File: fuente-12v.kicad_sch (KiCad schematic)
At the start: 36 parts, among them Q1 IPP65R190C7, Q2 CSD16403Q5A, U1 UCC287501D, U2 TCMT1107, U3 TL432DBZ, U4 TPS24701DGKR

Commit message: Esquematico completo y PCB routeado
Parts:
- removed C6: C, symbol Device:C_Polarized
- removed D1: D_Schottky, Package_TO_SOT_THT:TO-220-2_Vertical, symbol Device:D_Schottky
- added C13, C19: 10n, Capacitor_SMD:C_0805_2012Metric_Pad1.18x1.45mm_HandSolder, symbol Device:C
- added C14: 100uF, Capacitor_THT:CP_Radial_D8.0mm_P3.80mm, symbol Device:C
- added C15: 4.7uF 50V, Capacitor_SMD:C_0805_2012Metric_Pad1.18x1.45mm_HandSolder, symbol Device:C
- added C16: 470nF, Capacitor_SMD:C_0805_2012Metric_Pad1.18x1.45mm_HandSolder, symbol Device:C
- added C17: 470nF 400V, Capacitor_THT:C_Disc_D14.5mm_W5.0mm_P7.50mm, symbol Device:C
- added C20: 33nF X2, Capacitor_THT:C_Rect_L11.5mm_W6.6mm_P10.00mm_MKT, symbol Device:C
- added C21, C23: 100nF, Capacitor_SMD:C_0805_2012Metric_Pad1.18x1.45mm_HandSolder, symbol Device:C
- added C22: 470pF, Capacitor_SMD:C_0805_2012Metric_Pad1.18x1.45mm_HandSolder, symbol Device:C
- added C24: 10nF, Capacitor_SMD:C_1206_3216Metric_Pad1.33x1.80mm_HandSolder, symbol Device:C
- added C25, C26: 1nF Y1, Capacitor_THT:C_Disc_D10.5mm_W5.0mm_P10.00mm, symbol Device:C
- added C27: 22pF 50V, Capacitor_SMD:C_0805_2012Metric_Pad1.18x1.45mm_HandSolder, symbol Device:C
- added C29: 150uF 400V, Capacitor_THT:CP_Radial_D18.0mm_P7.50mm, symbol Device:C_Polarized
- added D1: GREEN, LED_SMD:LED_0805_2012Metric_Pad1.15x1.40mm_HandSolder, symbol Device:LED
- added D2, D3, D4, D5: 1N4148WT, Diode_SMD:D_SOD-523, symbol Diode:1N4148WT
- added D6: MBR20200CT, Package_TO_SOT_THT:TO-220-3_Vertical, symbol Device:D_Schottky_AKA
- added D7: Bzt52c20, Diode_SMD:Nexperia_CFP3_SOD-123W, symbol Device:D_Zener
- added D8: ES1J, Diode_SMD:D_SMA_Handsoldering, symbol Device:D
- added D9: KBL10, Diode_THT:Diode_Bridge_19.0x3.5x10.0mm_P5.0mm, symbol Device:D_Bridge_+AA-
- added F1: 1A 20mm, Fuse:Fuseholder_Cylinder-5x20mm_Schurter_0031_8201_Horizontal_Open, symbol Device:Fuse
- added FL1: ST-110BH, fuente-12v:ST-110, symbol Device:Filter_EMI_LL
- added J1: Conn_01x03_Pin, Connector_PinHeader_2.54mm:PinHeader_1x03_P2.54mm_Vertical, symbol Connector:Conn_01x03_Pin
- added J2: Screw_Terminal_01x03, TerminalBlock:TerminalBlock_MaiXu_MX126-5.0-03P_1x03_P5.00mm, symbol Connector:Screw_Terminal_01x03
- added J3: Conn_01x02_Pin, Connector_PinHeader_2.54mm:PinHeader_1x02_P2.54mm_Horizontal, symbol Connector:Conn_01x02_Pin
- added J5: OUTPUT, TerminalBlock:TerminalBlock_MaiXu_MX126-5.0-02P_1x02_P5.00mm, symbol Connector:Screw_Terminal_01x02
- added J6: Screw_Terminal_01x03 P5mm, TerminalBlock:TerminalBlock_MaiXu_MX126-5.0-03P_1x03_P5.00mm, symbol Connector:Screw_Terminal_01x03
- added R16: 0.018, Resistor_SMD:R_2512_6332Metric_Pad1.40x3.35mm_HandSolder, symbol Device:R
- added R17: 1M, Resistor_THT:R_Axial_DIN0207_L6.3mm_D2.5mm_P10.16mm_Horizontal, symbol Device:R
- added R18, R19: 2M, Resistor_SMD:R_0805_2012Metric_Pad1.20x1.40mm_HandSolder, symbol Device:R
- added R20, R21, R27: 10, Resistor_SMD:R_0805_2012Metric_Pad1.20x1.40mm_HandSolder, symbol Device:R
- added R22: 22, Resistor_SMD:R_1206_3216Metric_Pad1.30x1.75mm_HandSolder, symbol Device:R
- added R23: 80k, Resistor_SMD:R_1206_3216Metric_Pad1.30x1.75mm_HandSolder, symbol Device:R
- added R24: 6.8k, Resistor_SMD:R_0805_2012Metric_Pad1.20x1.40mm_HandSolder, symbol Device:R
- added R26: 10k, Resistor_SMD:R_0805_2012Metric_Pad1.20x1.40mm_HandSolder, symbol Device:R
- added RA1, RB1: 220, Resistor_SMD:R_0805_2012Metric_Pad1.20x1.40mm_HandSolder, symbol Device:R
- added RV1: 1k, Potentiometer_THT:Potentiometer_Bourns_3266Y_Vertical, symbol Device:R_Potentiometer_Trim
- added RV2: Varistor, Capacitor_THT:C_Disc_D8.0mm_W2.5mm_P5.00mm, symbol Device:Varistor
- added TP1, TP2, TP3, TP5, TP6, TP7, TP8, TP9: TestPoint, Connector_PinHeader_1.00mm:PinHeader_1x01_P1.00mm_Vertical, symbol Connector:TestPoint
- added U5: NE555P, Package_DIP:DIP-8_W7.62mm, symbol Timer:NE555P
- C1, C9: value C -> 680pF; footprint (none) -> Capacitor_SMD:C_0805_2012Metric_Pad1.18x1.45mm_HandSolder
- C10: value C -> 56pF; footprint (none) -> Capacitor_SMD:C_0805_2012Metric_Pad1.18x1.45mm_HandSolder
- C11: value C -> 1nF; footprint (none) -> Capacitor_SMD:C_0805_2012Metric_Pad1.18x1.45mm_HandSolder
- C12: value C -> 56nF; footprint (none) -> Capacitor_SMD:C_0805_2012Metric_Pad1.18x1.45mm_HandSolder
- C2, C3, C7: value C -> 4.7uF; footprint (none) -> Capacitor_SMD:C_1206_3216Metric_Pad1.33x1.80mm_HandSolder
- C4, C5: value C -> 470u; footprint (none) -> Capacitor_THT:CP_Radial_D13.0mm_P5.00mm
- C8: value 1nF -> 1nF Y1; footprint (none) -> Capacitor_THT:C_Disc_D16.0mm_W5.0mm_P10.00mm
- L1: value L -> 10uH 3A; footprint (none) -> Inductor_THT:L_Toroid_Vertical_L16.0mm_W8.0mm_P7.62mm
- R1: value R -> 10; footprint (none) -> Resistor_SMD:R_0805_2012Metric_Pad1.20x1.40mm_HandSolder
- R10: value R -> 5k; footprint (none) -> Resistor_SMD:R_0805_2012Metric_Pad1.20x1.40mm_HandSolder
- R11: value R -> 133k; footprint (none) -> Resistor_SMD:R_0805_2012Metric_Pad1.20x1.40mm_HandSolder
- R12: value R -> 2.49k; footprint (none) -> Resistor_SMD:R_0805_2012Metric_Pad1.20x1.40mm_HandSolder
- R13: value R -> 120k; footprint (none) -> Resistor_SMD:R_0805_2012Metric_Pad1.20x1.40mm_HandSolder
- R14, R5: value R -> 10k; footprint (none) -> Resistor_SMD:R_0805_2012Metric_Pad1.20x1.40mm_HandSolder
- R15: value R -> 0.018; footprint (none) -> Resistor_SMD:R_2512_6332Metric_Pad1.40x3.35mm_HandSolder
- R2, R4: value R -> 0.47; footprint (none) -> Resistor_SMD:R_2512_6332Metric_Pad1.40x3.35mm_HandSolder
- R3: value R -> 2M; footprint (none) -> Resistor_SMD:R_0805_2012Metric_Pad1.20x1.40mm_HandSolder
- R6: value R -> 100; footprint (none) -> Resistor_SMD:R_0805_2012Metric_Pad1.20x1.40mm_HandSolder
- R7: value R -> 51; footprint (none) -> Resistor_SMD:R_0805_2012Metric_Pad1.20x1.40mm_HandSolder
- R8: value R -> 86.6k; footprint (none) -> Resistor_SMD:R_0805_2012Metric_Pad1.20x1.40mm_HandSolder
- R9: value R -> 23.4k; footprint (none) -> Resistor_SMD:R_0805_2012Metric_Pad1.20x1.40mm_HandSolder
- T1: footprint (none) -> fuente-12v:750811744
- U4: footprint Package_TO_SOT_SMD:TSOT-23-6_HandSoldering -> Package_SO:VSSOP-8_2.3x2mm_P0.5mm
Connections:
- net FB: now also TP7.1
- net SECGND: now also R9.1, C16.1, J5.1 (Pin_1)
- net 12V: now reaches C5.1, L1.2, R14.2, R15.2, R7.2, U4.8 (VCC)
- net 12V: now also C3.2, R16.2, R24.1, TP3.1; no longer C7.2
- net at Q1.1 (G), R5.2: now also J1.2 (Pin_2); no longer R1.2
- net at Q1.2 (D), T1.2, T1.3: now also D8.2 (A)
- net P_GND: now reaches R2.2, R4.2
- net P_GND: now also C11.1, C8.1, R1.1, R5.1, T1.6, U1.1 (GND), U2.3, C13.2, C14.2, C15.2, C17.2, C19.2, C21.2, C23.2, C27.1, C29.2, D7.2 (A), D9.4 (-), J2.2 (Pin_2), J3.1 (Pin_1), R17.2, U5.1 (GND); no longer Q1.3 (S)
- net at C10.1, U3.1 (REF): now also C9.1, R8.1, R9.2, TP8.1; no longer R9.1
- net at C1.2, C2.2, C4.1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: now also C7.2, D6.2 (K); no longer C3.2
- net at R6.1, T1.10, T1.11: now also D6.1 (A), D6.3 (A), TP5.1
- net VOUT: now reaches Q2.1 (S), Q2.2 (S), Q2.3 (S), U4.5 (OUT)
- net VOUT: now also C16.2, J5.2 (Pin_2), TP6.1
- net at U4.6 (GATE): now also R27.1; no longer Q2.4 (G)
- net at Q2.5 (D), R15.1, U4.7 (SENSE): now also R16.1
- net at U4.1 (PGb): now also D1.1 (K)
- net at R4.1: now also Q1.3 (S), R2.1, R26.1, TP2.1; no longer U1.4 (CS)
- net at R3.1, U1.5 (VDD): now also C15.1, C21.1, D5.1 (K), D7.1 (K)
- net at U1.6 (DRV): now also R21.2; no longer R1.1
- net at R10.2, R12.2, U2.1: now also TP9.1
- net LINE_DC: now reaches T1.4, T1.5
- net LINE_DC: now also C24.1, J2.3 (Pin_3), R19.2, R23.1, TP1.1
- net VAUX: now reaches T1.7
- net VAUX: now also C22.1, D4.2 (A)
- net at R3.2: now also R18.1
- removed net GND: C11.1, C8.1, R2.1, R5.1, U1.1 (GND), U2.3
- new net: C14.1, D5.2 (A), R20.1
- new net: R18.2, R19.1
- new net: J1.3 (Pin_3), R21.1
- new net: Q2.4 (G), R27.2
- new net: C20.2, C25.1, F1.2, FL1.1, RV2.1
- new net: RB1.1, RV1.1
- new net: RA1.2, RV1.3
- new net: C27.2, R26.2, U1.4 (CS)
- new net: D3.1 (K), RB1.2
- new net: C24.2, R22.2, R23.2
- new net: D9.2, FL1.2
- new net: D9.3, FL1.4
- new net: D8.1 (K), R22.1
- new net: T1.1, T1.14
- new net: D4.1 (K), R20.2
- new net: D1.2 (A), R24.2
- new net: C22.2, R1.2
- new net: C19.1, U5.5 (CV)
- new net +5V: C23.1, J3.2 (Pin_2), RA1.1, U5.8 (VCC)
- new net 5V: U5.4 (R)
- new net AUX_DRV: J1.1 (Pin_1), U5.3 (Q)
- new net DIS: D2.2 (A), RV1.2, U5.7 (DIS)
- new net GNDPWR: C25.2, C26.1, J6.3 (Pin_3)
- new net L: F1.1, J6.1 (Pin_1)
- new net MAINS_LINE_DC: C17.1, C29.1, D9.1 (+), J2.1 (Pin_1), R17.1
- new net N: C20.1, C26.2, FL1.3, J6.2 (Pin_2), RV2.2
- new net TRIG: C13.1, D2.1 (K), D3.2 (A), U5.2 (TR), U5.6 (THR)
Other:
- note added: "Controlador Hotswap"
- note added: "Entrada Auxiliar de 311V"
- note added: "Generador Auxiliar de PWM"
- title: (none) -> Fuente Flyback 12V 2.5A
- moved on the sheet: C1, C10, C11, C12, C2, C3, C4, C7, C8, C9, Q1, Q2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

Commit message: Terminada. Necesita revision
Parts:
- added H1, H2, H3, H4: MountingHole, MountingHole:MountingHole_4.3mm_M4_DIN965, symbol Mechanical:MountingHole
- added TP10, TP11, TP4: TestPoint, Connector_PinHeader_1.00mm:PinHeader_1x01_P1.00mm_Vertical, symbol Connector:TestPoint
- C1: renamed from C8; now left out of the parts list
- C2: renamed from C29; now left out of the parts list
- C3: renamed from C17; now left out of the parts list
- C4: renamed from C5; now left out of the parts list
- C5: renamed from C25; now left out of the parts list
- C6: renamed from C20; now left out of the parts list
- C7: renamed from C26; now left out of the parts list
- C8: renamed from C14; now left out of the parts list
- C9: renamed from C4; now left out of the parts list
- D1: renamed from D9; now left out of the parts list
- D2: renamed from D6; now left out of the parts list
- F1, FL1, L1, Q1, T1, TP1, TP5: now left out of the parts list
- J1: renamed from J2; now left out of the parts list
- J2: renamed from J6; now left out of the parts list
- J3: renamed from J1; now left out of the parts list
- J4: renamed from J5; now left out of the parts list
- J5: renamed from J3; now left out of the parts list
- R1: renamed from R17; now left out of the parts list
- RV1: renamed from RV2; now left out of the parts list
- RV2: renamed from RV1; now left out of the parts list
- TP2: renamed from TP3; now left out of the parts list
- TP3: renamed from TP6; now left out of the parts list
- TP6: renamed from TP2; now left out of the parts list
- TP7: renamed from TP8; now left out of the parts list
- TP8: renamed from TP9; now left out of the parts list
- TP9: renamed from TP7; now left out of the parts list
- U1: renamed from U5; now left out of the parts list
- U4: renamed from U2; now left out of the parts list
- renumbered C22 to C10, C16 to C11, C3 to C13, C24 to C14, C2 to C15, C7 to C16, C1 to C17, C19 to C18, C9 to C19, C10 to C20, C11 to C21, C21 to C22, C27 to C23, C15 to C24, C13 to C25, C23 to C26, D1 to D3, D8 to D4, D4 to D5, D5 to D6, D2 to D8, D3 to D9, R22 to R10, R6 to R11, R3 to R12, R18 to R13, R19 to R14, R7 to R15, R9 to R16, R10 to R17, R12 to R18, R11 to R19, R24 to R2, R8 to R20, R5 to R21, R21 to R22, R20 to R23, R2 to R24, R4 to R25, RA1 to R27, RB1 to R28, R1 to R3, R23 to R4, R16 to R5, R13 to R6, R14 to R7, R15 to R8, R27 to R9, U4 to U2, U1 to U5
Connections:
- net 5V is gone; now on net +5V: U1.4 (R)
- net VAUX: now also TP11.1
- net at C22.1, C24.1, D6.1 (K)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: now also TP10.1
- net at J3.2 (Pin_2), Q1.1 (G), R21.2: now also TP4.1
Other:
- moved on the sheet: R28

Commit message: Version enviada a JLCPCB
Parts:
- added C27: 33nF X2, Capacitor_THT:C_Rect_L11.5mm_W6.6mm_P10.00mm_MKT, symbol Device:C
- added R29: 1M, Resistor_SMD:R_1206_3216Metric_Pad1.30x1.75mm_HandSolder, symbol Device:R
- F1: footprint Fuse:Fuseholder_Cylinder-5x20mm_Schurter_0031_8201_Horizontal_Open -> fuente-12v:Fuseholder_BLX-A
- R1: footprint Resistor_THT:R_Axial_DIN0207_L6.3mm_D2.5mm_P10.16mm_Horizontal -> Resistor_SMD:R_1206_3216Metric_Pad1.30x1.75mm_HandSolder
- T1: value ~ -> 750811744
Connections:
- net N: no longer C7.2
- net P_GND: now also C1.2, R29.2; no longer C1.1, R1.2
- net at C6.2, F1.2, FL1.1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: no longer C5.1
- net at D1.2, FL1.2: now also C5.1, C27.2
- net at D1.3, FL1.4: now also C7.2, C27.1
- net SECGND renamed S_GND
- net S_GND: now also C1.1; no longer C1.2
- new net: R1.2, R29.1
- no-connect marks 0 -> 2
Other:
- note added: "Aislación por PCB Slot"
- note added: "Entrada Auxiliar de DC"
- note added: "Entrada de Red"
- note added: "Puentear 1 con 3 para operacion normal"
- note removed: "Entrada Auxiliar de 311V"
- moved on the sheet: C1, C10, C11, C12, C13, C14, C15, C16, C17, C18, C19, C2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

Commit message: initial commit
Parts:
- removed C18, C25: 10n, Capacitor_SMD:C_0805_2012Metric_Pad1.18x1.45mm_HandSolder, symbol Device:C
- removed C26: 100nF, Capacitor_SMD:C_0805_2012Metric_Pad1.18x1.45mm_HandSolder, symbol Device:C
- removed D8, D9: 1N4148WT, Diode_SMD:D_SOD-523, symbol Diode:1N4148WT
- removed J5: Conn_01x02_Pin, Connector_PinHeader_2.54mm:PinHeader_1x02_P2.54mm_Horizontal, symbol Connector:Conn_01x02_Pin
- removed R28: 220, Resistor_SMD:R_0805_2012Metric_Pad1.20x1.40mm_HandSolder, symbol Device:R
- removed RV2: 1k, Potentiometer_THT:Potentiometer_Bourns_3266Y_Vertical, symbol Device:R_Potentiometer_Trim
- removed U1: NE555P, Package_DIP:DIP-8_W7.62mm, symbol Timer:NE555P
- C24: value 4.7uF 50V -> 10uF 50V
- D1: footprint Diode_THT:Diode_Bridge_19.0x3.5x10.0mm_P5.0mm -> Diode_THT:Diode_Bridge_Vishay_KBL
- D5, D6: footprint Diode_SMD:D_SOD-523 -> Diode_SMD:D_SOD-323_HandSoldering
- R27: value 220 -> 470
- TP1, TP10, TP11, TP2, TP3, TP4, TP5, TP6, TP7, TP8, TP9: footprint Connector_PinHeader_1.00mm:PinHeader_1x01_P1.00mm_Vertical -> Connector_PinHeader_2.54mm:PinHeader_1x01_P2.54mm_Vertical
- U2: footprint Package_SO:VSSOP-8_2.3x2mm_P0.5mm -> Package_SO:Texas_S-PDSO-G8_3x3mm_P0.65mm
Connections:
- net +5V is gone; now on net S_GND: R27.1
- net 12V: now also R27.2
- net S_GND: now also T1.10, T1.11; no longer T1.12, T1.13
- net at D2.1 (A), D2.3 (A), R11.1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: now also T1.12, T1.13; no longer T1.10, T1.11
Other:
- note removed: "Generador Auxiliar de PWM"

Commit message: V2 routeada por bruno, necesita revision
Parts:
- removed J3: Conn_01x03_Pin, Connector_PinHeader_2.54mm:PinHeader_1x03_P2.54mm_Vertical, symbol Connector:Conn_01x03_Pin
- removed TP3: TestPoint, Connector_PinHeader_2.54mm:PinHeader_1x01_P2.54mm_Vertical, symbol Connector:TestPoint
- added J5: Conn_01x02_Pin, Connector_PinHeader_2.54mm:PinHeader_1x02_P2.54mm_Vertical, symbol Connector:Conn_01x02_Pin
- added R28, R30, R31, R32: 2M, Resistor_SMD:R_0805_2012Metric_Pad1.20x1.40mm_HandSolder, symbol Device:R
- R4: footprint Resistor_SMD:R_1206_3216Metric_Pad1.30x1.75mm_HandSolder -> Resistor_THT:R_Axial_DIN0411_L9.9mm_D3.6mm_P15.24mm_Horizontal
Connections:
- net LINE_DC: now also R32.2
- net P_GND: now also R30.1
- net at Q1.1 (G), R21.2, TP4.1: now also J5.1 (Pin_1)
- net at R22.1: now also J5.2 (Pin_2)
- net at U5.3 (FLT): now also R28.1, R30.2
- new net: R28.2, R31.1
- new net: R31.2, R32.1
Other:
- moved on the sheet: C10, C2, C22, C24, C27, C3, C5, C6, C7, C8, D1, D5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

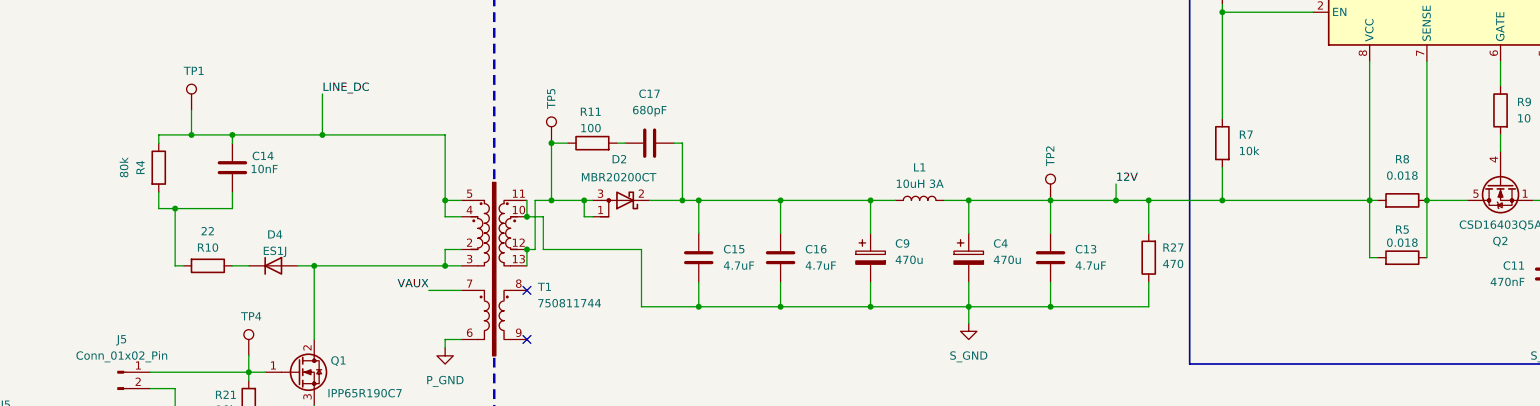
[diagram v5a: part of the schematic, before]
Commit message: Correcciones en el esquemático
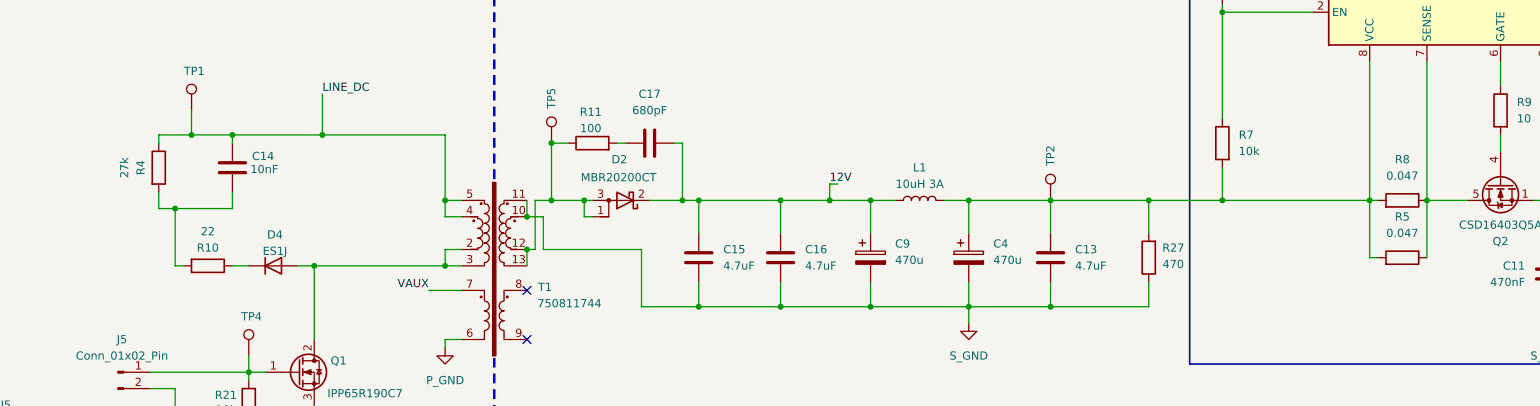
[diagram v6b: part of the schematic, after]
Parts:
- R4: value 80k -> 27k
- R5, R8: value 0.018 -> 0.047
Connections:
- net 12V: now also C15.2, C16.2, C17.2, C9.1, D2.2 (K), L1.1; no longer C13.2, C4.1, L1.2, R27.2, R5.2, R7.2, R8.2, TP2.1, U2.8 (VCC)
- new net: C13.2, C4.1, L1.2, R27.2, R5.2, R7.2, R8.2, TP2.1, U2.8 (VCC)
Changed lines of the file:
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@@
 	)
 	(junction
-		(at 300.99 110.49)
-		(diameter 0)
-		(color 0 0 0 0)
-	)
-	(junction
 		(at 236.22 127)
 		(diameter 0)
@@
 	)
 	(junction
+		(at 256.54 110.49)
+		(diameter 0)
+		(color 0 0 0 0)
+	)
+	(junction
 		(at 218.44 191.77)
 		(diameter 0)
@@
 	(wire
 		(pts
+			(xy 256.54 110.49) (xy 262.89 110.49)
+		)
+		(stroke
+			(width 0)
+			(type default)
+		)
+	)
+	(wire
+		(pts
 			(xy 247.65 228.6) (xy 247.65 219.71)
 		)
@@
 	(wire
 		(pts
+			(xy 340.36 119.38) (xy 341.63 119.38)
+		)
+		(stroke
+			(width 0)
+			(type default)
+		)
+	)
+	(wire
+		(pts
 			(xy 139.7 157.48) (xy 142.24 157.48)
 		)
@@
 	(wire
 		(pts
-			(xy 349.25 110.49) (xy 349.25 119.38)
-		)
-		(stroke
-			(width 0)
-			(type default)
-		)
-	)
-	(wire
-		(pts
 			(xy 176.53 167.64) (xy 176.53 168.91)
 		)
@@
 	(wire
 		(pts
-			(xy 300.99 110.49) (xy 306.07 110.49)
-		)
-		(stroke
-			(width 0)
-			(type default)
-		)
-	)
-	(wire
-		(pts
 			(xy 330.2 71.12) (xy 331.47 71.12)
 		)
@@
 	(wire
 		(pts
-			(xy 176.53 157.48) (xy 176.53 160.02)
+			(xy 340.36 110.49) (xy 340.36 119.38)
 		)
 		(stroke
@@
 	(wire
 		(pts
-			(xy 262.89 110.49) (xy 248.92 110.49)
+			(xy 176.53 157.48) (xy 176.53 160.02)
 		)
 		(stroke
@@
 	(wire
 		(pts
+			(xy 256.54 107.95) (xy 257.81 107.95)
+		)
+		(stroke
+			(width 0)
+			(type default)
+		)
+	)
+	(wire
+		(pts
 			(xy 199.39 132.08) (xy 196.85 132.08)
 		)
@@
 	(wire
 		(pts
-			(xy 300.99 107.95) (xy 300.99 110.49)
+			(xy 256.54 107.95) (xy 256.54 110.49)
 		)
 		(stroke
@@
 	(wire
 		(pts
+			(xy 349.25 110.49) (xy 349.25 119.38)
+		)
+		(stroke
+			(width 0)
+			(type default)
+		)
+	)
+	(wire
+		(pts
 			(xy 31.75 149.86) (xy 31.75 153.67)
 		)
@@
 	(wire
 		(pts
-			(xy 340.36 119.38) (xy 341.63 119.38)
-		)
-		(stroke
-			(width 0)
-			(type default)
-		)
-	)
-	(wire
-		(pts
 			(xy 191.77 214.63) (xy 191.77 217.17)
 		)
@@
 	(wire
 		(pts
-			(xy 223.52 101.6) (xy 224.79 101.6)
+			(xy 248.92 110.49) (xy 256.54 110.49)
 		)
 		(stroke
@@
 	(wire
 		(pts
-			(xy 290.83 110.49) (xy 300.99 110.49)
+			(xy 223.52 101.6) (xy 224.79 101.6)
 		)
 		(stroke
@@
 	(wire
 		(pts
-			(xy 93.98 58.42) (xy 93.98 60.96)
+			(xy 290.83 110.49) (xy 306.07 110.49)
 		)
 		(stroke
@@
 	(wire
 		(pts
-			(xy 340.36 110.49) (xy 340.36 119.38)
+			(xy 93.98 58.42) (xy 93.98 60.96)
 		)
 		(stroke
@@
 	)
 	(label "12V"
-		(at 300.99 107.95 0)
+		(at 256.54 107.95 0)
 		(effects
 			(font
@@
 	)
 	(symbol
+		(lib_id "Device:R")
+		(at 345.44 119.38 270)
+		(mirror x)
+		(unit 1)
+		(exclude_from_sim no)
+		(in_bom yes)
+		(on_board yes)
+		(dnp no)
+		(fields_autoplaced yes)
+		(property "Reference" "R5"
+			(at 345.44 113.03 90)
+			(effects
+				(font
+					(size 1.27 1.27)
+				)
+			)
+		)
+		(property "Value" "0.047"
+			(at 345.44 115.57 90)
+			(effects
+				(font
+					(size 1.27 1.27)
+				)
+			)
+		)
+		(property "Footprint" "Resistor_SMD:R_2512_6332Metric_Pad1.40x3.35mm_HandSolder"
+			(at 345.44 121.158 90)
+			(effects
+				(font
+					(size 1.27 1.27)
+				)
+				(hide yes)
+			)
+		)
+		(property "Datasheet" "~"
+			(at 345.44 119.38 0)
+			(effects
+				(font
+					(size 1.27 1.27)
+				)
+				(hide yes)
+			)
+		)
+		(property "Description" "https://www.dicomse.com.ar/"
+			(at 345.44 119.38 0)
+			(effects
+				(font
+					(size 1.27 1.27)
+				)
+				(hide yes)
+			)
+		)
+		(pin "2"
+		)
+		(pin "1"
+		)
+		(instances
+			(project "fuente-12v"
+				(path "/55d2e28b-83a0-4cce-b804-0834af0209d7"
+					(reference "R5")
+					(unit 1)
+				)
+			)
+		)
+	)
+	(symbol
 		(lib_id "Device:D_Schottky_AKA")
 		(at 224.79 110.49 180)
@@
 			)
 		)
-		(property "Value" "80k"
+		(property "Value" "27k"
 			(at 147.066 105.41 90)
 			(effects
@@
 			)
 		)
-		(property "Value" "0.018"
+		(property "Value" "0.047"
 			(at 345.44 106.68 90)
 			(effects
@@
 					(unit 1)
 				)
-			)
-		)
-	)
-	(symbol
-		(lib_id "Device:R")
-		(at 345.44 119.38 270)
-		(mirror x)
-		(unit 1)
-		(exclude_from_sim no)
-		(in_bom yes)
-		(on_board yes)
-		(dnp no)
-		(property "Reference" "R5"
-			(at 345.44 115.062 90)
-			(effects
-				(font
-					(size 1.27 1.27)
-				)
-			)
-		)
-		(property "Value" "0.018"
-			(at 345.44 117.094 90)
-			(effects
-				(font
-					(size 1.27 1.27)
-				)
-			)
-		)
-		(property "Footprint" "Resistor_SMD:R_2512_6332Metric_Pad1.40x3.35mm_HandSolder"
-			(at 345.44 121.158 90)
-			(effects
-				(font
-					(size 1.27 1.27)
-				)
-				(hide yes)
-			)
-		)
-		(property "Datasheet" "~"
-			(at 345.44 119.38 0)
-			(effects
-				(font
-					(size 1.27 1.27)
-				)
-				(hide yes)
-			)
-		)
-		(property "Description" "https://www.dicomse.com.ar/"
-			(at 345.44 119.38 0)
-			(effects
-				(font
-					(size 1.27 1.27)
-				)
-				(hide yes)
-			)
-		)
-		(pin "2"
-		)
-		(pin "1"
-		)
-		(instances
-			(project "fuente-12v"
-				(path "/55d2e28b-83a0-4cce-b804-0834af0209d7"
-					(reference "R5")
-					(unit 1)
-				)

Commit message: Cambios v2
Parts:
- R25: value 0.47 -> DNP
- R26: value 10k -> 1k
- R5: value 0.047 -> DNP
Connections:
- net 12V: no longer R2.1
- net 12V_FILT: now reaches C13.2, C4.1, L1.2, R27.2, R5.2, R7.2, R8.2, TP2.1, U2.8 (VCC)
- net 12V_FILT: now also R2.1
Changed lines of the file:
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@@
 	)
 	(junction
-		(at 256.54 110.49)
-		(diameter 0)
-		(color 0 0 0 0)
-	)
-	(junction
 		(at 218.44 191.77)
 		(diameter 0)
@@
 	)
 	(junction
+		(at 281.94 110.49)
+		(diameter 0)
+		(color 0 0 0 0)
+	)
+	(junction
 		(at 62.23 31.75)
 		(diameter 0)
@@
 	(wire
 		(pts
-			(xy 256.54 110.49) (xy 262.89 110.49)
-		)
-		(stroke
-			(width 0)
-			(type default)
-		)
-	)
-	(wire
-		(pts
 			(xy 247.65 228.6) (xy 247.65 219.71)
 		)
@@
 	(wire
 		(pts
+			(xy 281.94 110.49) (xy 290.83 110.49)
+		)
+		(stroke
+			(width 0)
+			(type default)
+		)
+	)
+	(wire
+		(pts
 			(xy 74.93 36.83) (xy 78.74 36.83)
 		)
@@
 	(wire
 		(pts
-			(xy 256.54 107.95) (xy 257.81 107.95)
-		)
-		(stroke
-			(width 0)
-			(type default)
-		)
-	)
-	(wire
-		(pts
 			(xy 199.39 132.08) (xy 196.85 132.08)
 		)
@@
 	(wire
 		(pts
-			(xy 256.54 107.95) (xy 256.54 110.49)
+			(xy 248.92 107.95) (xy 248.92 110.49)
 		)
 		(stroke
@@
 	(wire
 		(pts
-			(xy 278.13 110.49) (xy 290.83 110.49)
+			(xy 278.13 110.49) (xy 281.94 110.49)
 		)
 		(stroke
@@
 	(wire
 		(pts
+			(xy 248.92 110.49) (xy 262.89 110.49)
+		)
+		(stroke
+			(width 0)
+			(type default)
+		)
+	)
+	(wire
+		(pts
 			(xy 290.83 127) (xy 306.07 127)
 		)
@@
 	(wire
 		(pts
-			(xy 248.92 110.49) (xy 256.54 110.49)
-		)
-		(stroke
-			(width 0)
-			(type default)
-		)
-	)
-	(wire
-		(pts
 			(xy 223.52 101.6) (xy 224.79 101.6)
 		)
@@
 	(wire
 		(pts
+			(xy 281.94 107.95) (xy 281.94 110.49)
+		)
+		(stroke
+			(width 0)
+			(type default)
+		)
+	)
+	(wire
+		(pts
 			(xy 227.33 127) (xy 236.22 127)
 		)
@@
 		)
 	)
+	(label "12V"
+		(at 248.92 107.95 0)
+		(effects
+			(font
+				(size 1.27 1.27)
+			)
+			(justify left bottom)
+		)
+	)
 	(label "FB"
 		(at 114.3 162.56 0)
@@
 		)
 	)
-	(label "VOUT"
-		(at 384.81 110.49 0)
+	(label "12V_FILT"
+		(at 383.54 53.34 0)
 		(effects
 			(font
@@
 		)
 	)
-	(label "12V"
-		(at 383.54 53.34 0)
+	(label "VOUT"
+		(at 384.81 110.49 0)
 		(effects
 			(font
@@
 		)
 	)
-	(label "12V"
-		(at 256.54 107.95 0)
+	(label "12V_FILT"
+		(at 281.94 107.95 0)
 		(effects
 			(font
@@
 			)
 		)
-		(property "Value" "0.047"
+		(property "Value" "DNP"
 			(at 345.44 115.57 90)
 			(effects
@@
 			)
 		)
-		(property "Value" "10k"
+		(property "Value" "1k"
 			(at 151.384 163.068 90)
 			(effects
@@
 			)
 		)
-		(property "Value" "0.47"
+		(property "Value" "DNP"
 			(at 188.976 165.1 0)
 			(effects

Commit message: V2 fabricada
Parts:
- added TP12, TP13, TP14, TP3: TestPoint, Connector_PinHeader_2.54mm:PinHeader_1x01_P2.54mm_Vertical, symbol Connector:TestPoint
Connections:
- net P_GND: now also TP12.1, TP3.1
- net S_GND: now also TP13.1
- net at C23.2, R26.2, U5.4 (CS): now also TP14.1
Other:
- moved on the sheet: C23
